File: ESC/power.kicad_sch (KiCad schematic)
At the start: 1 part, among them J1 Conn_01x02_Socket

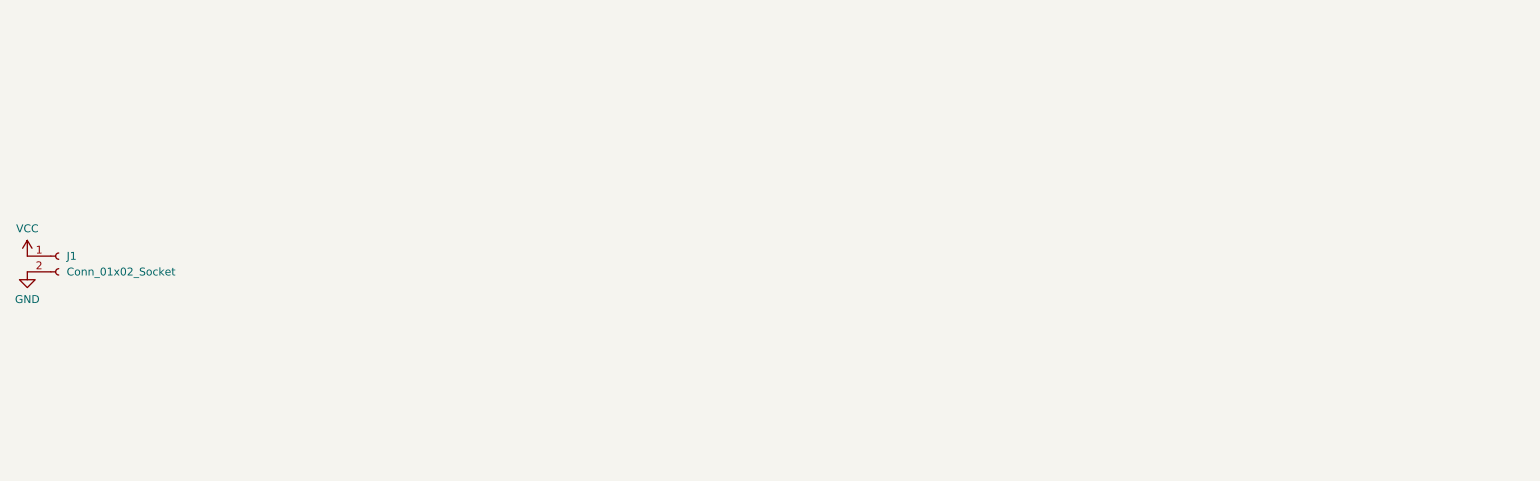
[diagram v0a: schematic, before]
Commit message: added pictures of daq board, updated esc to finish on three phase control
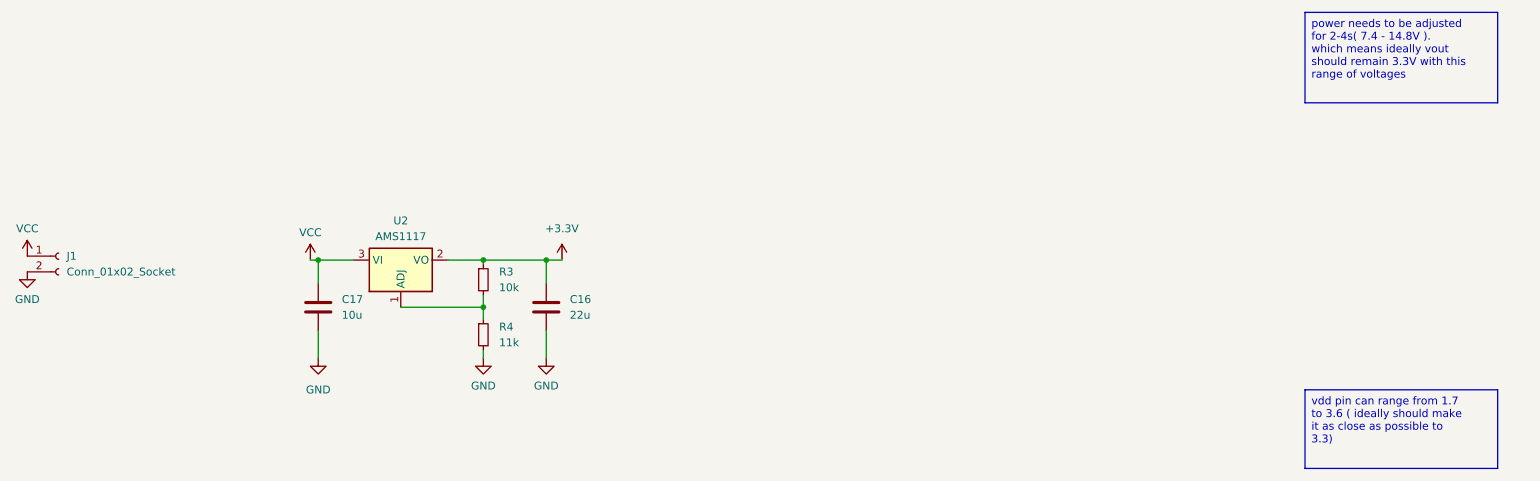
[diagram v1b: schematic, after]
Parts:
- added C16: 22u, symbol Device:C
- added C17: 10u, symbol Device:C
- added R3: 10k, symbol Device:R_Small
- added R4: 11k, symbol Device:R_Small
- added U2: AMS1117, Package_TO_SOT_SMD:SOT-223-3_TabPin2, symbol Regulator_Linear:AMS1117
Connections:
- net GND: now also C16.2, C17.2, R4.2
- net VCC: now also C17.1, U2.3 (VI)
- new net: R3.2, R4.1, U2.1 (ADJ)
- new net +3.3V: C16.1, R3.1, U2.2 (VO)

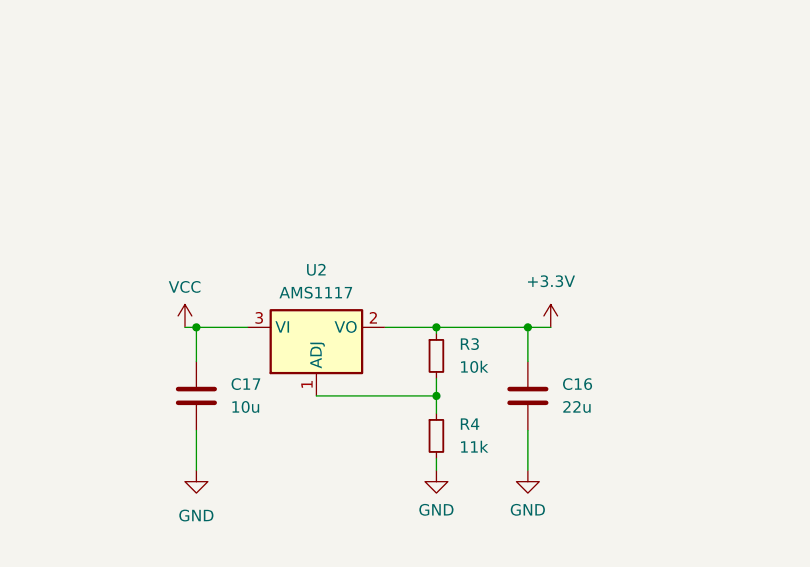
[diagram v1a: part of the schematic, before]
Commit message: finished first mock up of the esc scheamtic still need to check everything works tho
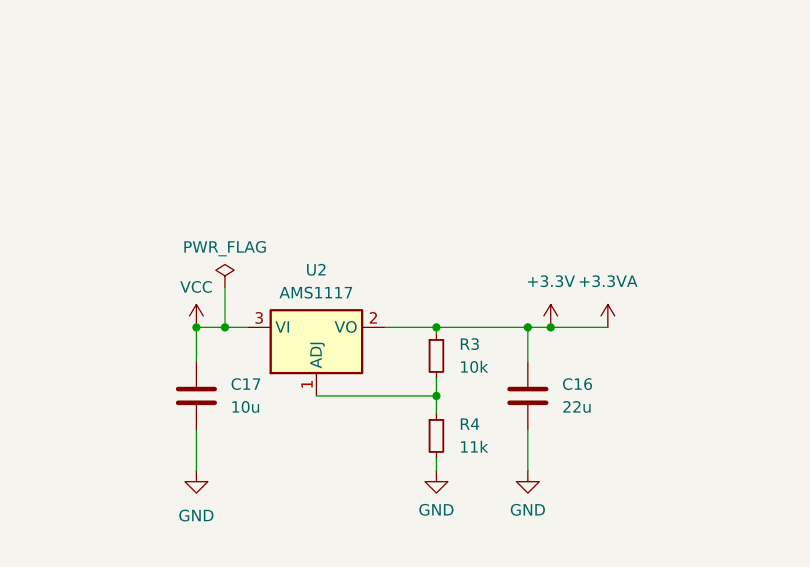
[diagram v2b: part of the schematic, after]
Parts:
- C16, C17: footprint (none) -> Capacitor_SMD:C_0603_1608Metric_Pad1.08x0.95mm_HandSolder
- R3, R4: footprint (none) -> Resistor_SMD:R_0603_1608Metric_Pad0.98x0.95mm_HandSolder
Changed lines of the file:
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@@
   (junction (at 119.38 53.34) (diameter 0) (color 0 0 0 0)
   )
+  (junction (at 132.08 53.34) (diameter 0) (color 0 0 0 0)
+  )
+  (junction (at 95.885 53.34) (diameter 0) (color 0 0 0 0)
+  )
   (junction (at 92.71 53.34) (diameter 0) (color 0 0 0 0)
   )
@@
     (stroke (width 0) (type default))
   )
+  (wire (pts (xy 132.08 53.34) (xy 138.43 53.34))
+    (stroke (width 0) (type default))
+  )
+  (wire (pts (xy 113.665 53.34) (xy 119.38 53.34))
+    (stroke (width 0) (type default))
+  )
   (wire (pts (xy 129.54 64.77) (xy 129.54 69.215))
     (stroke (width 0) (type default))
@@
     (stroke (width 0) (type default))
   )
-  (wire (pts (xy 92.71 53.34) (xy 98.425 53.34))
+  (wire (pts (xy 95.885 48.895) (xy 95.885 53.34))
     (stroke (width 0) (type default))
   )
-  (wire (pts (xy 91.44 53.34) (xy 92.71 53.34))
+  (wire (pts (xy 92.71 53.34) (xy 95.885 53.34))
     (stroke (width 0) (type default))
   )
@@
     (stroke (width 0) (type default))
   )
-  (wire (pts (xy 113.665 53.34) (xy 119.38 53.34))
+  (wire (pts (xy 95.885 53.34) (xy 98.425 53.34))
     (stroke (width 0) (type default))
   )
@@
     (effects (font (size 1.27 1.27)) (justify left top))
   )
+  (symbol (lib_id "power:PWR_FLAG") (at 95.885 48.895 0) (unit 1)
+    (in_bom yes) (on_board yes) (dnp no) (fields_autoplaced)
+    (property "Reference" "#FLG01" (at 95.885 46.99 0)
+      (effects (font (size 1.27 1.27)) hide)
+    )
+    (property "Value" "PWR_FLAG" (at 95.885 44.45 0)
+      (effects (font (size 1.27 1.27)))
+    )
+    (property "Footprint" "" (at 95.885 48.895 0)
+      (effects (font (size 1.27 1.27)) hide)
+    )
+    (property "Datasheet" "~" (at 95.885 48.895 0)
+      (effects (font (size 1.27 1.27)) hide)
+    )
+    (pin "1")
+    (instances
+      (project "ESC"
+        (path "/88e9b63e-ca06-4d41-87b7-50146fa458bf/19277d6f-6fa4-4d47-97bb-6cdb890a6ffd"
+          (reference "#FLG01") (unit 1)
+        )
+      )
+    )
+  )
   (symbol (lib_id "Connector:Conn_01x02_Socket") (at 50.8 52.705 0) (unit 1)
     (in_bom yes) (on_board yes) (dnp no) (fields_autoplaced)
@@
       (effects (font (size 1.27 1.27)) (justify left))
     )
-    (property "Footprint" "" (at 119.38 65.405 0)
+    (property "Footprint" "Resistor_SMD:R_0603_1608Metric_Pad0.98x0.95mm_HandSolder" (at 119.38 65.405 0)
       (effects (font (size 1.27 1.27)) hide)
     )
@@
     )
   )
+  (symbol (lib_id "power:+3.3VA") (at 138.43 53.34 0) (unit 1)
+    (in_bom yes) (on_board yes) (dnp no) (fields_autoplaced)
+    (property "Reference" "#PWR015" (at 138.43 57.15 0)
+      (effects (font (size 1.27 1.27)) hide)
+    )
+    (property "Value" "+3.3VA" (at 138.43 48.26 0)
+      (effects (font (size 1.27 1.27)))
+    )
+    (property "Footprint" "" (at 138.43 53.34 0)
+      (effects (font (size 1.27 1.27)) hide)
+    )
+    (property "Datasheet" "" (at 138.43 53.34 0)
+      (effects (font (size 1.27 1.27)) hide)
+    )
+    (pin "1")
+    (instances
+      (project "ESC"
+        (path "/88e9b63e-ca06-4d41-87b7-50146fa458bf/19277d6f-6fa4-4d47-97bb-6cdb890a6ffd"
+          (reference "#PWR015") (unit 1)
+        )
+      )
+    )
+  )
   (symbol (lib_id "power:VCC") (at 45.72 52.705 0) (unit 1)
     (in_bom yes) (on_board yes) (dnp no) (fields_autoplaced)
@@
       (effects (font (size 1.27 1.27)) (justify left))
     )
-    (property "Footprint" "" (at 119.38 56.515 0)
+    (property "Footprint" "Resistor_SMD:R_0603_1608Metric_Pad0.98x0.95mm_HandSolder" (at 119.38 56.515 0)
       (effects (font (size 1.27 1.27)) hide)
     )
@@
       (effects (font (size 1.27 1.27)) (justify left))
     )
-    (property "Footprint" "" (at 130.5052 64.77 0)
+    (property "Footprint" "Capacitor_SMD:C_0603_1608Metric_Pad1.08x0.95mm_HandSolder" (at 130.5052 64.77 0)
       (effects (font (size 1.27 1.27)) hide)
     )
@@
     )
   )
-  (symbol (lib_id "power:VCC") (at 91.44 53.34 0) (unit 1)
+  (symbol (lib_id "power:VCC") (at 92.71 53.34 0) (unit 1)
     (in_bom yes) (on_board yes) (dnp no) (fields_autoplaced)
-    (property "Reference" "#PWR024" (at 91.44 57.15 0)
+    (property "Reference" "#PWR024" (at 92.71 57.15 0)
       (effects (font (size 1.27 1.27)) hide)
     )
-    (property "Value" "VCC" (at 91.44 48.895 0)
+    (property "Value" "VCC" (at 92.71 48.895 0)
       (effects (font (size 1.27 1.27)))
     )
-    (property "Footprint" "" (at 91.44 53.34 0)
+    (property "Footprint" "" (at 92.71 53.34 0)
       (effects (font (size 1.27 1.27)) hide)
     )
-    (property "Datasheet" "" (at 91.44 53.34 0)
+    (property "Datasheet" "" (at 92.71 53.34 0)
       (effects (font (size 1.27 1.27)) hide)
     )
@@
       (effects (font (size 1.27 1.27)) (justify left))
     )
-    (property "Footprint" "" (at 93.6752 64.77 0)
+    (property "Footprint" "Capacitor_SMD:C_0603_1608Metric_Pad1.08x0.95mm_HandSolder" (at 93.6752 64.77 0)
       (effects (font (size 1.27 1.27)) hide)
     )

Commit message: finished a mockup of the pcb layout
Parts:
- J1: footprint Connector_AMASS:AMASS_XT60PW-M_1x02_P7.20mm_Horizontal -> Connector_AMASS:AMASS_XT60PW-F_1x02_P7.20mm_Horizontal
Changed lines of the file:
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@@
       (effects (font (size 1.27 1.27)) (justify left))
     )
-    (property "Footprint" "Connector_AMASS:AMASS_XT60PW-M_1x02_P7.20mm_Horizontal" (at 50.8 52.705 0)
+    (property "Footprint" "Connector_AMASS:AMASS_XT60PW-F_1x02_P7.20mm_Horizontal" (at 50.8 52.705 0)
       (effects (font (size 1.27 1.27)) hide)
     )
